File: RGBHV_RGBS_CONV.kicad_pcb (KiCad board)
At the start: 2 copper layers, 100 x 100 mm, 74 parts, among them J1 DIGITAL RGB, J10 AUDIO1, J11 RGBHV_2, J12 AUDIO2, J15 RGBS_OUT1, J16 RGBS_OUT2, J17 VIN, J2 VGA DB15, J3 ANALOG RGB DA15, J4 X1, J5 DIGITAL_RGBHV_1, J6 ANALOG RGB, J7 DIGITAL_RGBHV_2, J8 SWITCHER, J9 RGBHV_1, U1 OUT_GND_IN_3.3V, U2 74HC86, U3 OUT_IN_GND_3.3V

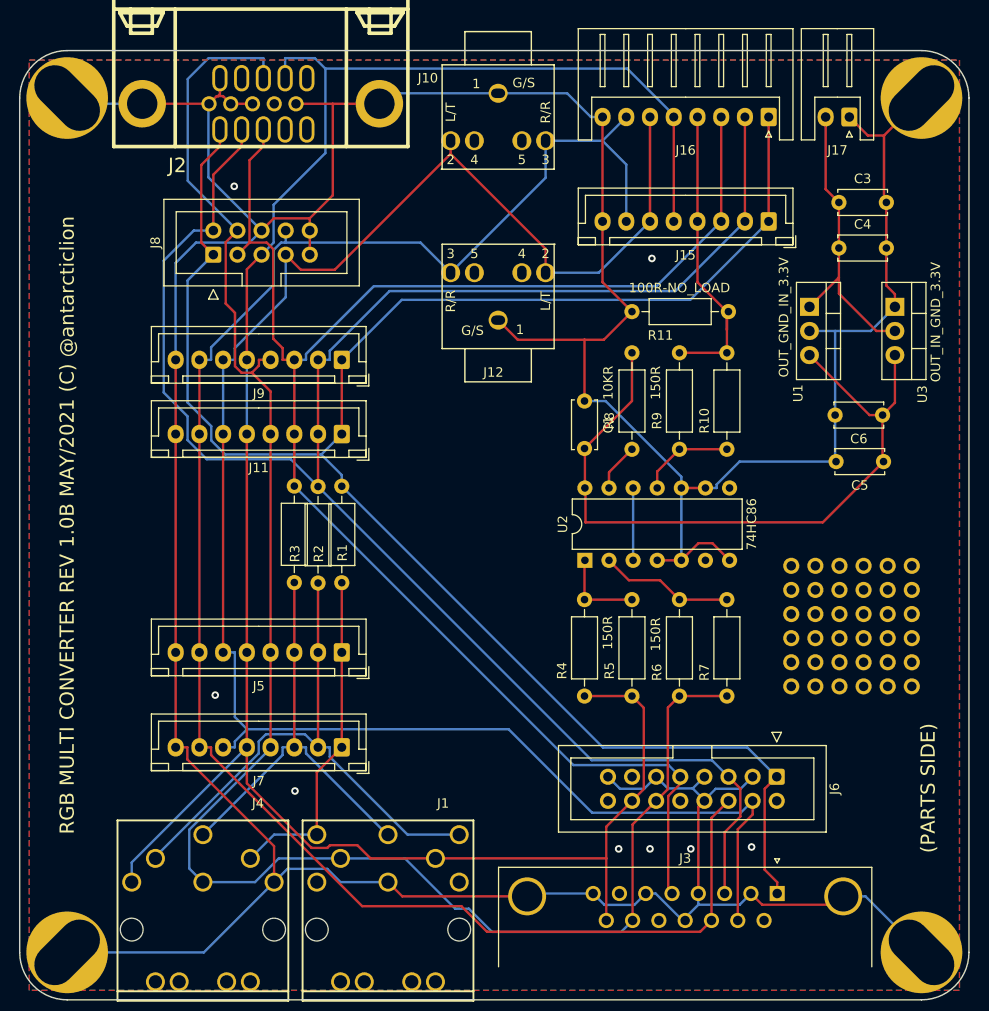
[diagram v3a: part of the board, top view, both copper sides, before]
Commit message: Rev1.0C
レギュレータのパターンを追加。
RGBS XHコネクタへの音声パターンカット
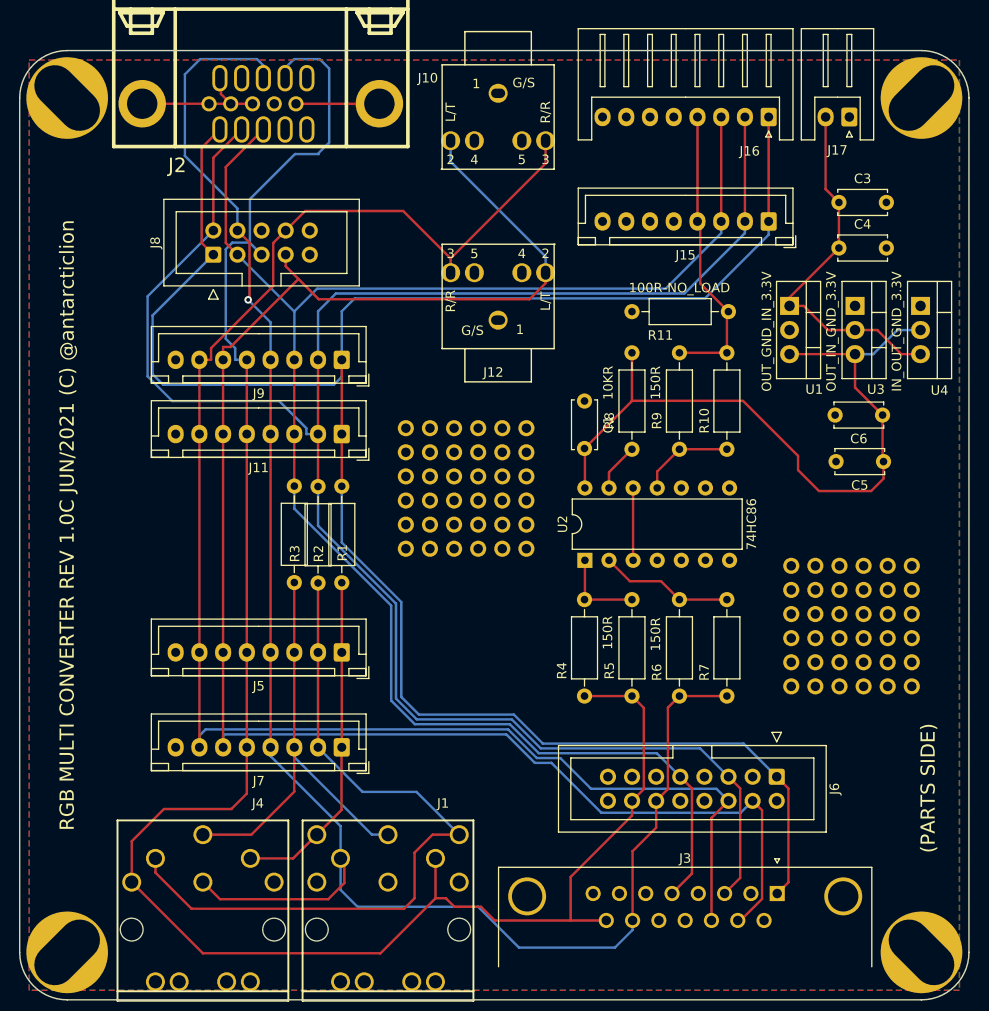
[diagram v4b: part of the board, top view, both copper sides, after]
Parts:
- added PIN01: Pin_2.54, ryuk_lib:Pin_2.54, F.Cu at (90.7, 101.8)
- added PIN02: Pin_2.54, ryuk_lib:Pin_2.54, F.Cu at (93.2, 101.8)
- added PIN03: Pin_2.54, ryuk_lib:Pin_2.54, F.Cu at (95.8, 101.8)
- added PIN04: Pin_2.54, ryuk_lib:Pin_2.54, F.Cu at (98.3, 101.8)
- added PIN05: Pin_2.54, ryuk_lib:Pin_2.54, F.Cu at (100.8, 101.8)
- added PIN06: Pin_2.54, ryuk_lib:Pin_2.54, F.Cu at (103.4, 101.8)
- added PIN07: Pin_2.54, ryuk_lib:Pin_2.54, F.Cu at (90.7, 104.3)
- added PIN08: Pin_2.54, ryuk_lib:Pin_2.54, F.Cu at (93.2, 104.3)
- added PIN09: Pin_2.54, ryuk_lib:Pin_2.54, F.Cu at (95.8, 104.3)
- added PIN10: Pin_2.54, ryuk_lib:Pin_2.54, F.Cu at (98.3, 104.3)
- added PIN11: Pin_2.54, ryuk_lib:Pin_2.54, F.Cu at (100.8, 104.3)
- added PIN12: Pin_2.54, ryuk_lib:Pin_2.54, F.Cu at (103.4, 104.3)
- added PIN13: Pin_2.54, ryuk_lib:Pin_2.54, F.Cu at (90.7, 106.9)
- added PIN14: Pin_2.54, ryuk_lib:Pin_2.54, F.Cu at (93.2, 106.9)
- added PIN15: Pin_2.54, ryuk_lib:Pin_2.54, F.Cu at (95.8, 106.9)
- added PIN16: Pin_2.54, ryuk_lib:Pin_2.54, F.Cu at (98.3, 106.9)
- added PIN17: Pin_2.54, ryuk_lib:Pin_2.54, F.Cu at (100.8, 106.9)
- added PIN18: Pin_2.54, ryuk_lib:Pin_2.54, F.Cu at (103.4, 106.9)
- added PIN19: Pin_2.54, ryuk_lib:Pin_2.54, F.Cu at (90.7, 109.4)
- added PIN20: Pin_2.54, ryuk_lib:Pin_2.54, F.Cu at (93.2, 109.4)
- added PIN21: Pin_2.54, ryuk_lib:Pin_2.54, F.Cu at (95.8, 109.4)
- added PIN22: Pin_2.54, ryuk_lib:Pin_2.54, F.Cu at (98.3, 109.4)
- added PIN23: Pin_2.54, ryuk_lib:Pin_2.54, F.Cu at (100.8, 109.4)
- added PIN24: Pin_2.54, ryuk_lib:Pin_2.54, F.Cu at (103.4, 109.4)
- added PIN25: Pin_2.54, ryuk_lib:Pin_2.54, F.Cu at (90.7, 111.9)
- added PIN26: Pin_2.54, ryuk_lib:Pin_2.54, F.Cu at (93.2, 111.9)
- added PIN27: Pin_2.54, ryuk_lib:Pin_2.54, F.Cu at (95.8, 111.9)
- added PIN28: Pin_2.54, ryuk_lib:Pin_2.54, F.Cu at (98.3, 111.9)
- added PIN29: Pin_2.54, ryuk_lib:Pin_2.54, F.Cu at (100.8, 111.9)
- added PIN30: Pin_2.54, ryuk_lib:Pin_2.54, F.Cu at (103.4, 111.9)
- added PIN31: Pin_2.54, ryuk_lib:Pin_2.54, F.Cu at (90.7, 114.5)
- added PIN32: Pin_2.54, ryuk_lib:Pin_2.54, F.Cu at (93.2, 114.5)
- added PIN33: Pin_2.54, ryuk_lib:Pin_2.54, F.Cu at (95.8, 114.5)
- added PIN34: Pin_2.54, ryuk_lib:Pin_2.54, F.Cu at (98.3, 114.5)
- added PIN35: Pin_2.54, ryuk_lib:Pin_2.54, F.Cu at (100.8, 114.5)
- added PIN36: Pin_2.54, ryuk_lib:Pin_2.54, F.Cu at (103.4, 114.5)
- added U4: IN_OUT_GND_3.3V, Package_TO_SOT_THT:TO-220-3_Vertical, F.Cu at (144.9, 88.9)
- moved U3 4.20 mm to (138.0, 88.9)
- moved U1 2.10 mm to (131.1, 88.9)
- renumbered PIN** to PIN01, PIN** to PIN02, PIN** to PIN03, PIN** to PIN04, PIN** to PIN05, PIN** to PIN06, PIN** to PIN07, PIN** to PIN08, PIN** to PIN09, PIN** to PIN10, PIN** to PIN11, PIN** to PIN12, PIN** to PIN13, PIN** to PIN14, PIN** to PIN15, PIN** to PIN16, PIN** to PIN17, PIN** to PIN18, PIN** to PIN19, PIN** to PIN20, PIN** to PIN21, PIN** to PIN22, PIN** to PIN23, PIN** to PIN24, PIN** to PIN25, PIN** to PIN26, PIN** to PIN27, PIN** to PIN28, PIN** to PIN29, PIN** to PIN30, PIN** to PIN31, PIN** to PIN32, PIN** to PIN33, PIN** to PIN34, PIN** to PIN35, PIN** to PIN36
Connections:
- J15 pad 5: VSYNC -> Net-(J15-Pad5)
- J15 pad 6: AUDIO_L -> Net-(J15-Pad6)
- J15 pad 7: AUDIO_R -> Net-(J15-Pad7)
- J16 pad 5: VSYNC -> Net-(J16-Pad5)
- J16 pad 6: AUDIO_L -> Net-(J16-Pad6)
- J16 pad 7: AUDIO_R -> Net-(J16-Pad7)
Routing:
- net GND: track 454.1 -> 23.6 mm, vias 8 -> 0
- net VSYNC: track 226.8 -> 204.9 mm
- net AUDIO_R: track 191.8 -> 171.0 mm
- net AUDIO_L: track 194.9 -> 178.2 mm
- net DIGITAL_G: track 60.5 -> 77.1 mm
- net R: track 197.5 -> 212.5 mm
- net G: track 199.5 -> 207.7 mm
- net Net-(C3-Pad1): track 31.1 -> 38.5 mm
- net B: track 172.4 -> 177.1 mm
- net DIGITAL_B: track 45.3 -> 47.8 mm
- net CSYNC: track 33.1 -> 31.3 mm
- net +3V3: track 76.1 -> 77.4 mm
- net HSYNC: track 188.6 -> 188.2 mm, vias 0 -> 1
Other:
- board text added: "1117"
- board text added: "48033"
- board text added: "7533-1"
- board text added: "RGB MULTI CONVERTER REV 1.0C JUN/2021 (C) @antarcticlion"
- board text removed: "RGB MULTI CONVERTER REV 1.0B MAY/2021 (C) @antarcticlion"

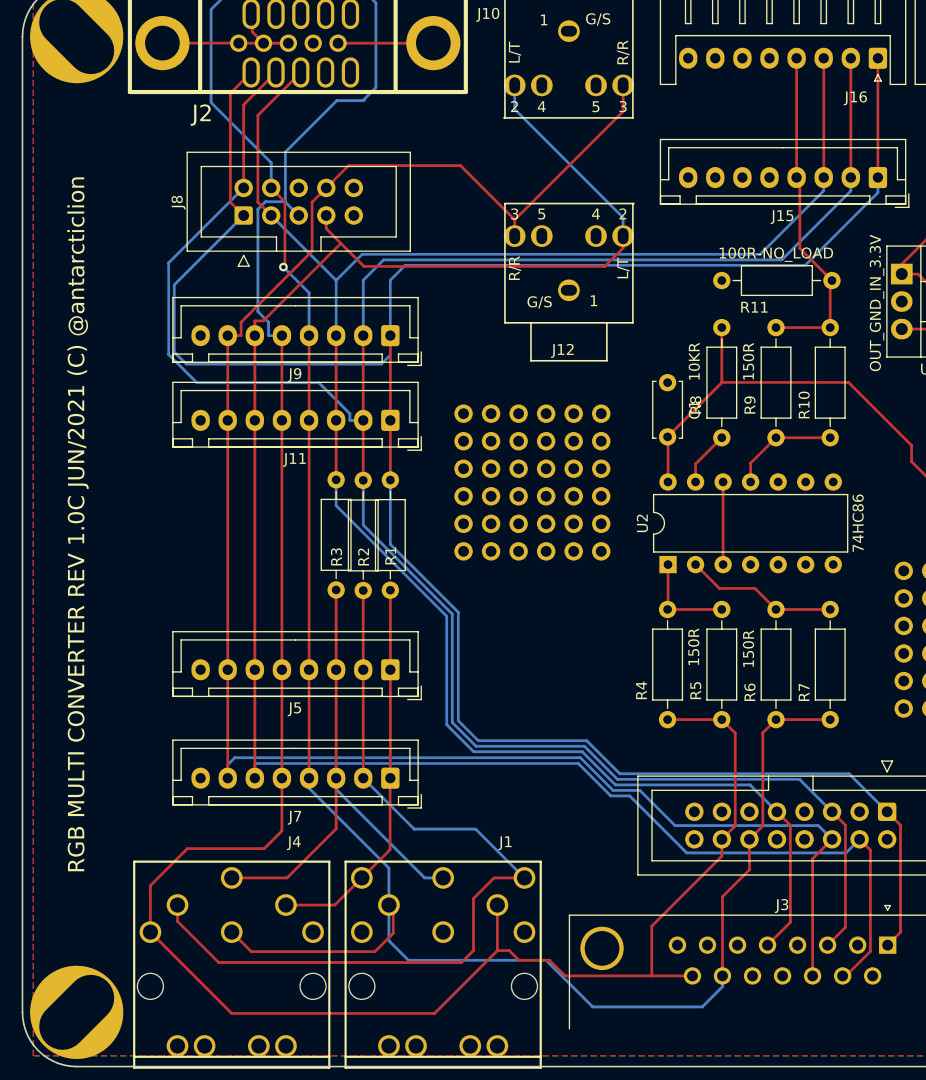
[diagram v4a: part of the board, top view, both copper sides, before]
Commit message: Rev 1.0D
Fix DIN8 R-G H-V pin swap bug
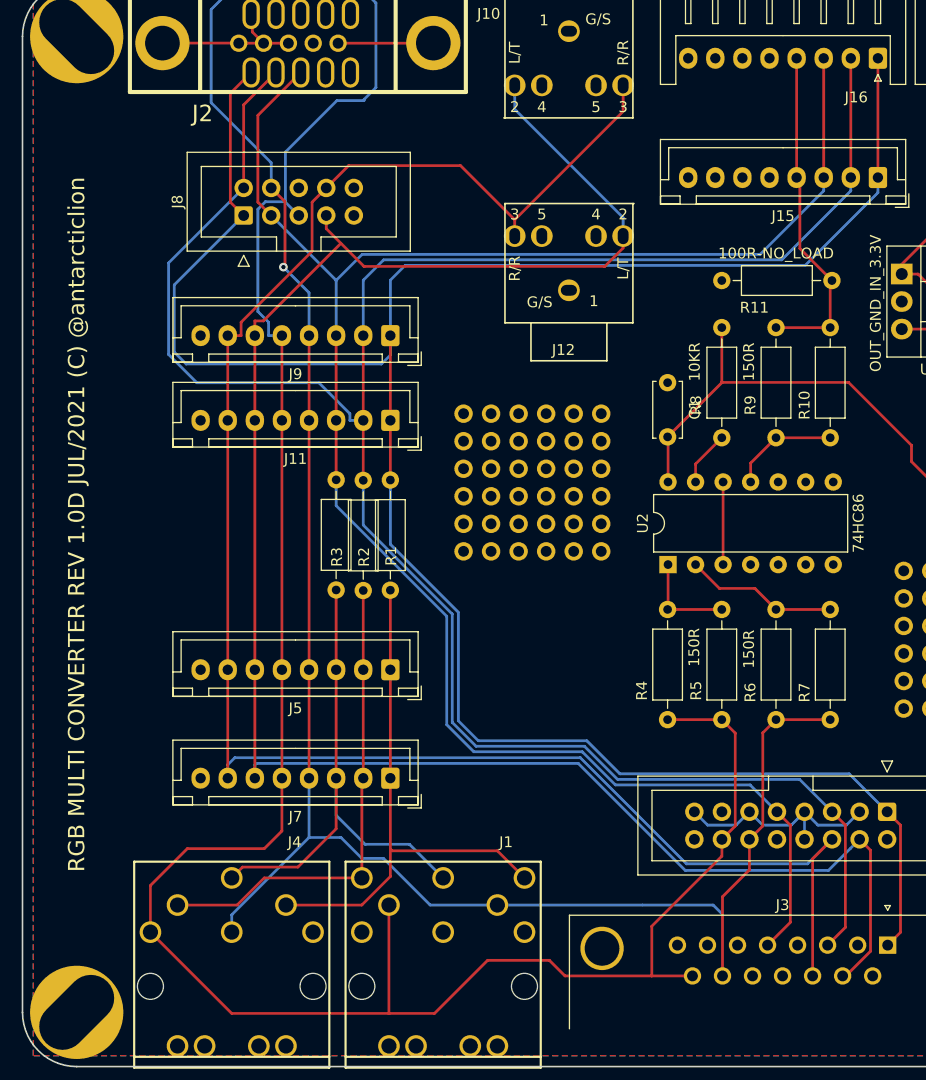
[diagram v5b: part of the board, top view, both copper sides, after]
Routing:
- net DIGITAL_G: track 77.1 -> 44.6 mm
- net GND: track 23.6 -> 44.4 mm
- net DIGITAL_R: track 35.7 -> 50.6 mm
- net HSYNC: track 188.2 -> 180.8 mm
- net VSYNC: track 204.9 -> 210.5 mm
- net AUDIO_R: track 171.0 -> 172.8 mm
- net DIGITAL_B: track 47.8 -> 49.2 mm
- net AUDIO_L: track 178.2 -> 179.6 mm
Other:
- board text added: "RGB MULTI CONVERTER REV 1.0D JUL/2021 (C) @antarcticlion"
- board text removed: "RGB MULTI CONVERTER REV 1.0C JUN/2021 (C) @antarcticlion"
